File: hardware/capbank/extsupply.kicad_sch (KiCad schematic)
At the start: 8 parts, among them U16 LM78L05ACZ

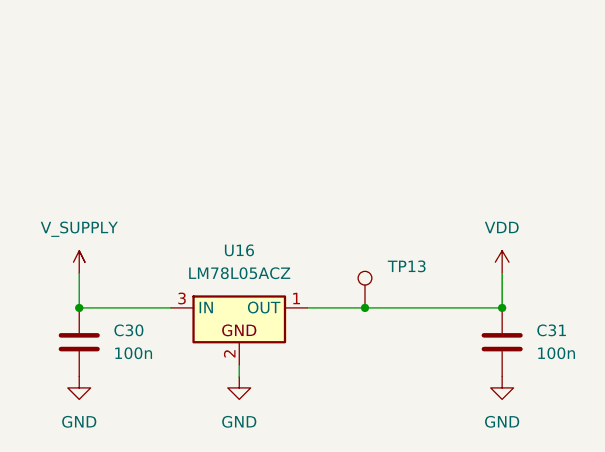
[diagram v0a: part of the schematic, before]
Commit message: Progress, layout nearly completed, build oscillator on breadboard
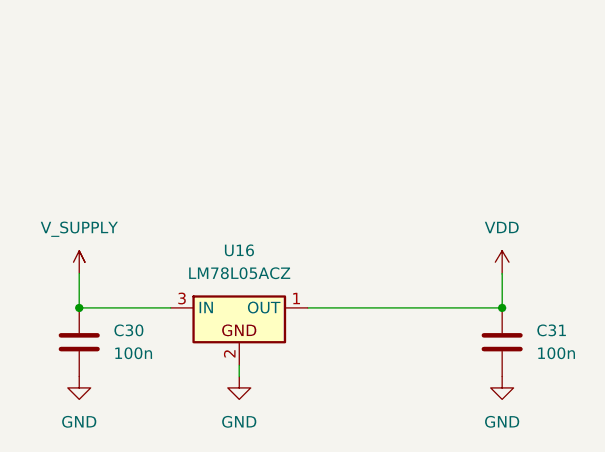
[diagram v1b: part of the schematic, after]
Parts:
- removed TP13: ~, TestPoint:TestPoint_THTPad_1.5x1.5mm_Drill0.7mm, symbol Connector:TestPoint
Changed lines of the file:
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@@
-	)
-	(junction
-		(at 172.72 80.01)
-		(diameter 0)
-		(color 0 0 0 0)
 	)
 	(junction
@@
 	(wire
 		(pts
-			(xy 172.72 80.01) (xy 187.96 80.01)
+			(xy 140.97 80.01) (xy 151.13 80.01)
 		)
 		(stroke
@@
 	(wire
 		(pts
-			(xy 140.97 80.01) (xy 151.13 80.01)
+			(xy 140.97 76.2) (xy 140.97 80.01)
 		)
 		(stroke
@@
 	(wire
 		(pts
-			(xy 140.97 76.2) (xy 140.97 80.01)
-		)
-		(stroke
-			(width 0)
-			(type default)
-		)
-	)
-	(wire
-		(pts
-			(xy 166.37 80.01) (xy 172.72 80.01)
+			(xy 166.37 80.01) (xy 187.96 80.01)
 		)
 		(stroke
@@
 					(unit 1)
 				)
-			)
-		)
-	)
-	(symbol
-		(lib_id "Connector:TestPoint")
-		(at 172.72 80.01 0)
-		(unit 1)
-		(exclude_from_sim no)
-		(in_bom yes)
-		(on_board yes)
-		(dnp no)
-		(property "Reference" "TP13"
-			(at 175.26 75.4379 0)
-			(effects
-				(font
-					(size 1.27 1.27)
-				)
-				(justify left)
-			)
-		)
-		(property "Value" "~"
-			(at 176.276 78.232 0)
-			(effects
-				(font
-					(size 1.27 1.27)
-				)
-				(justify left)
-			)
-		)
-		(property "Footprint" "TestPoint:TestPoint_THTPad_1.5x1.5mm_Drill0.7mm"
-			(at 177.8 80.01 0)
-			(effects
-				(font
-					(size 1.27 1.27)
-				)
-				(hide yes)
-			)
-		)
-		(property "Datasheet" "~"
-			(at 177.8 80.01 0)
-			(effects
-				(font
-					(size 1.27 1.27)
-				)
-				(hide yes)
-			)
-		)
-		(property "Description" "test point"
-			(at 172.72 80.01 0)
-			(effects
-				(font
-					(size 1.27 1.27)
-				)
-				(hide yes)
-			)
-		)
-		(pin "1"
-		)
-		(instances
-			(project "capbank1"
-				(path "/461cb8a1-2d60-44a8-88b5-d61a3ba14a84/05d9e891-8d4f-4840-a6ec-b10068883578"
-					(reference "TP13")
-					(unit 1)
-				)
